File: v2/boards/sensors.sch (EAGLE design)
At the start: 12 parts, among them U10 CNY70, U11 CNY70, U12 CNY70, U13 CNY70, U14 CNY70, U15 CNY70

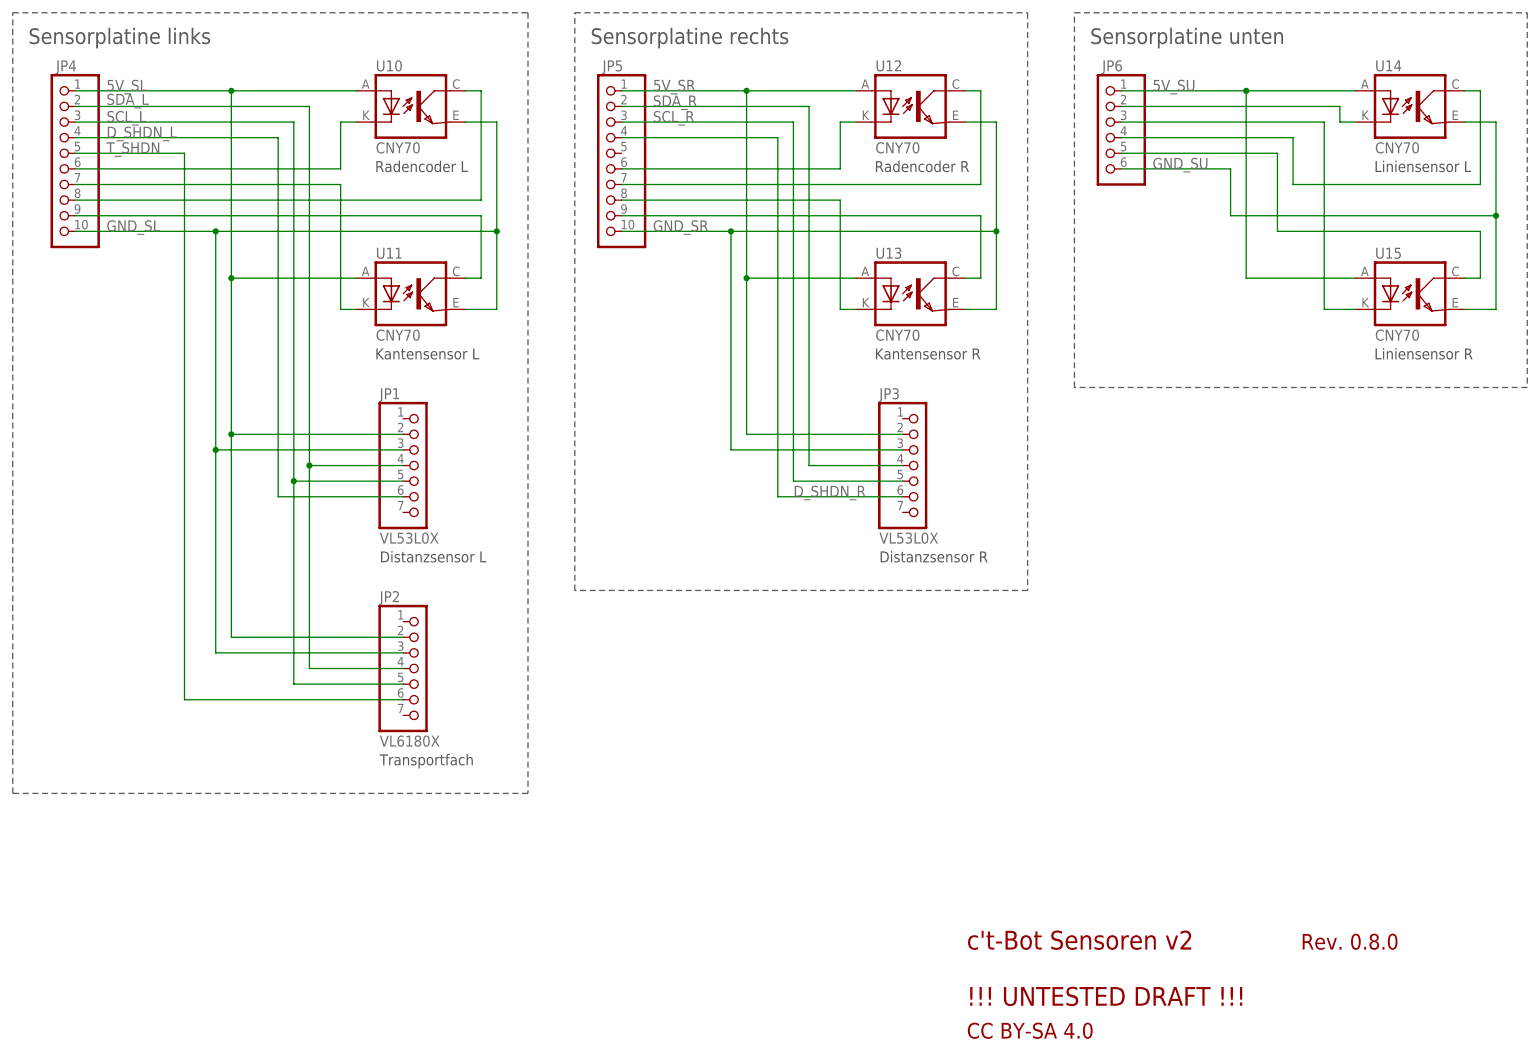
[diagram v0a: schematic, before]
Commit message: ct-bot v2 schematic updated
- optional current measurements added to mainboard
 - schematic drafts for sensor boards
 - pin mapping sheet updated (i2c-bus mapping)
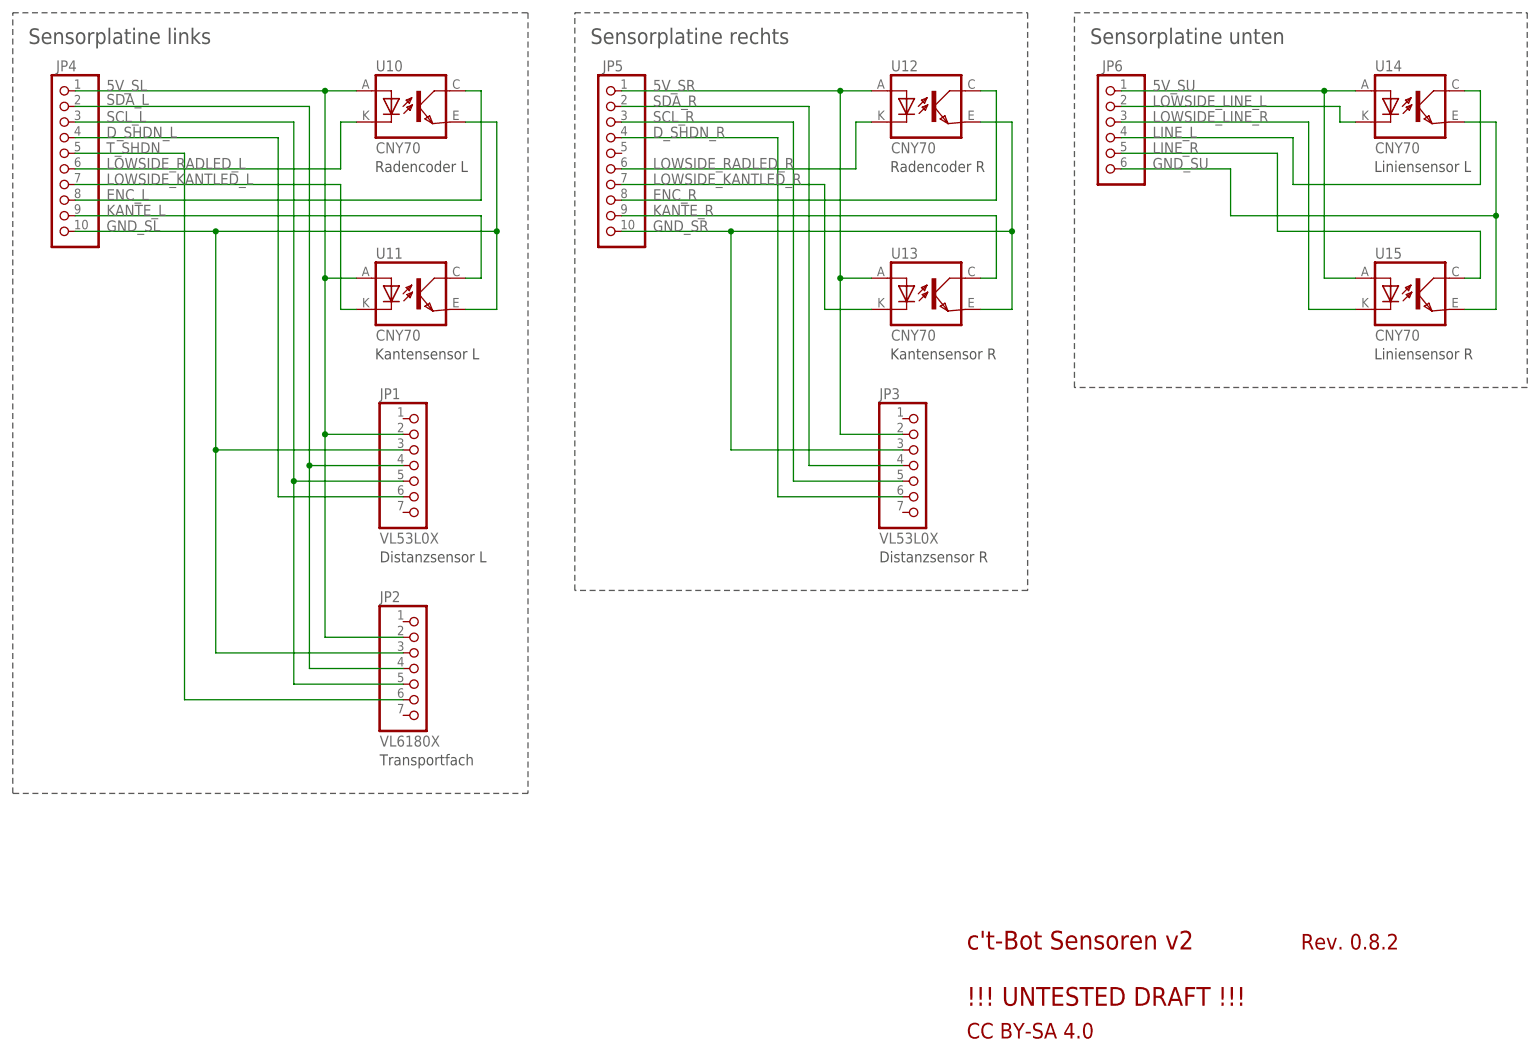
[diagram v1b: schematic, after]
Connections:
- net N$50 renamed LOWSIDE_RADLED_L
- net N$54 renamed ENC_L
- net N$55 renamed KANTE_L
- net N$56 renamed LOWSIDE_KANTLED_L
- net N$57 renamed LOWSIDE_RADLED_R
- net N$59 renamed KANTE_R
- net N$60 renamed LOWSIDE_LINE_L
- net N$61 renamed LOWSIDE_LINE_R
- net N$62 renamed LINE_L
- net N$63 renamed LINE_R
- removed net N$52: JP5.7, U12.COL
- removed net N$58: JP5.8, U13.C
- new net ENC_R: JP5.8, U12.COL
- new net LOWSIDE_KANTLED_R: JP5.7, U13.C
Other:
- note added: "Rev. 0.8.2"
- note removed: "Rev. 0.8.0"
- moved on the sheet: U12, U13
